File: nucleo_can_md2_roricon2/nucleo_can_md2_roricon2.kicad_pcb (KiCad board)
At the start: 2 copper layers, 63.7 x 58.6 mm, 24 parts, among them J1 Conn_01x05_Pin, J2 Conn_01x05_Pin, J3 Conn_01x02_Pin, U1 NUCLEO-F303K8, U2 MCP2562-E-P

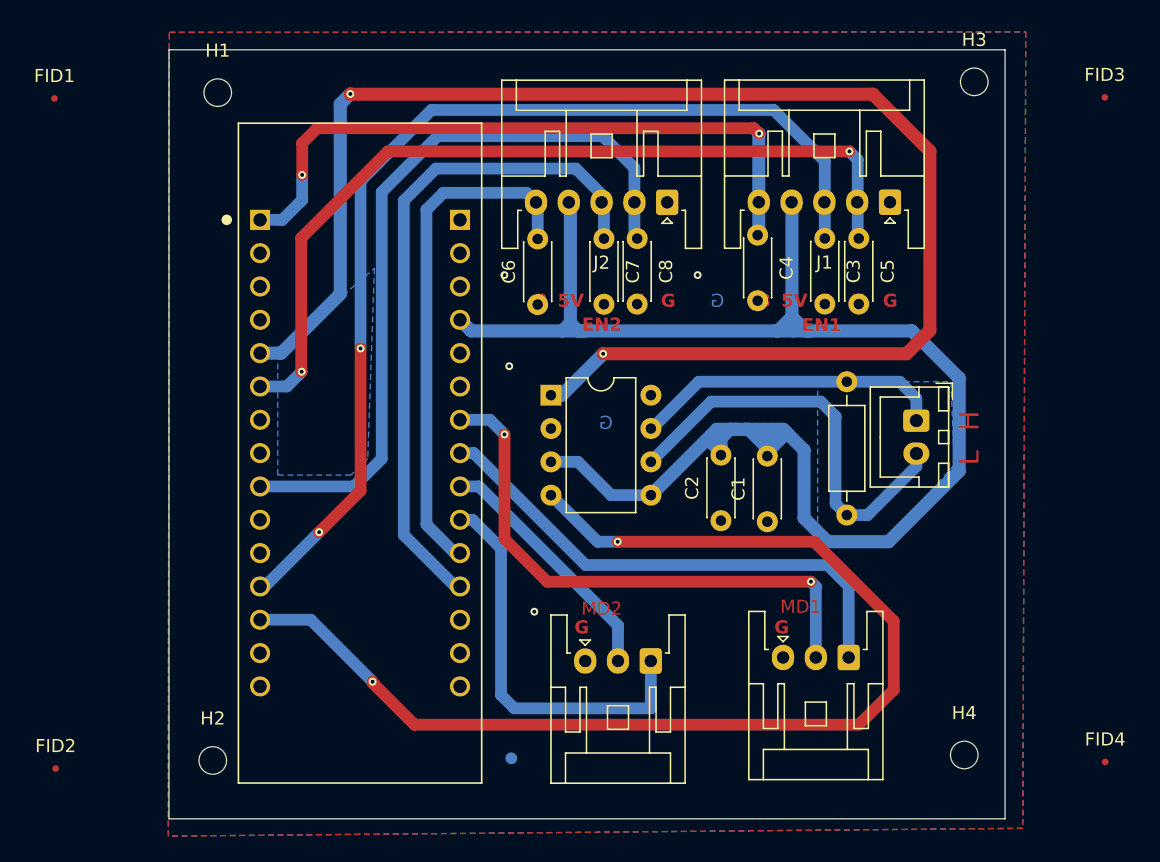
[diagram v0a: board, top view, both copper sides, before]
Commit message: feat:文字位置を修正
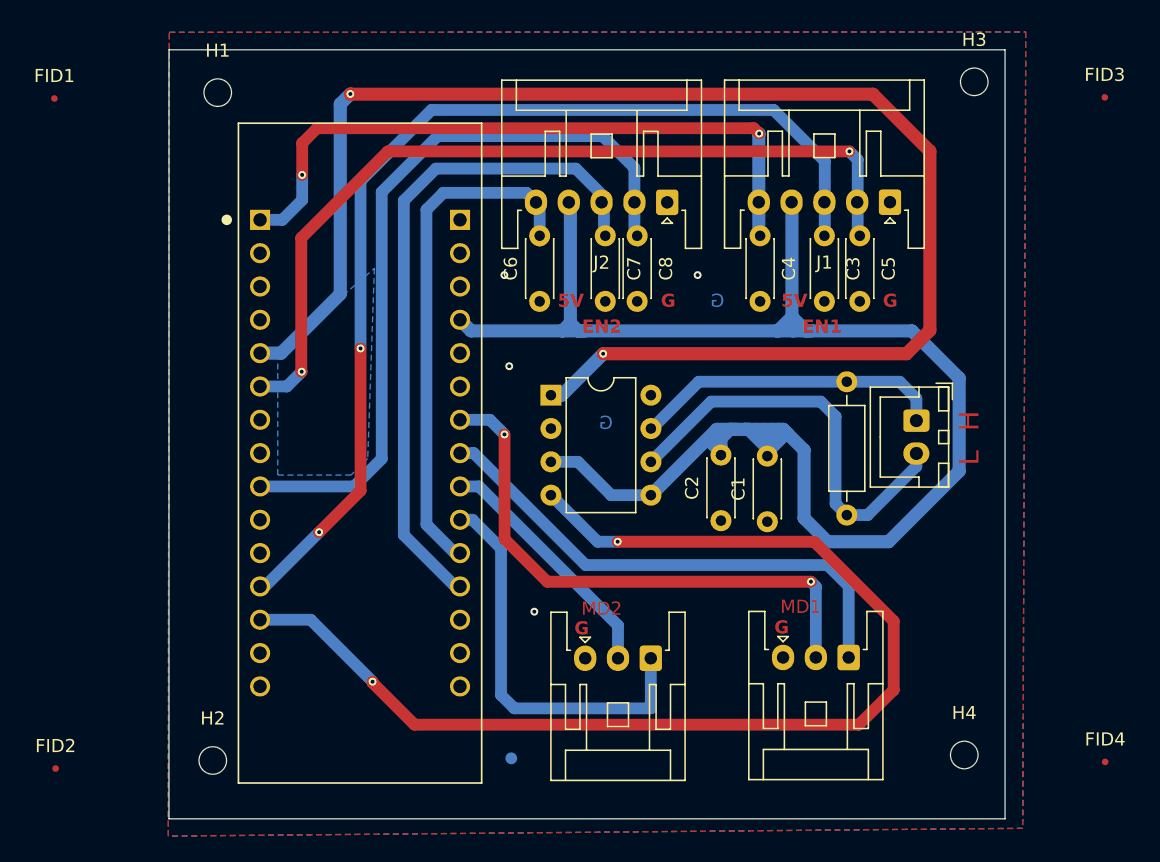
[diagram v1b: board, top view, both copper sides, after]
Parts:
- moved C6 0.29 mm to (142.9, 84.3)
- moved C7 0.24 mm to (147.9, 79.3)
- moved C5 0.22 mm to (167.3, 79.3)
- moved C8 0.21 mm to (150.3, 79.3)
- moved MD1 0.21 mm to (146.4, 111.5)
- moved C3 0.20 mm to (164.6, 79.3)
- moved C4 0.20 mm to (159.7, 79.3)
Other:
- board text removed: "A"
- board text removed: "B"
- board text removed: "X"
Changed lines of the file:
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@@
 	(footprint "Capacitor_THT:C_Disc_D4.3mm_W1.9mm_P5.00mm"
 		(layer "F.Cu")
-		(at 147.8 79.52 -90)
+		(at 147.9 79.3 -90)
 		(descr "C, Disc series, Radial, pin pitch=5.00mm, , diameter*width=4.3*1.9mm^2, Capacitor, http://www.vishay.com/docs/45233/krseries.pdf")
 		(tags "C Disc series Radial pin pitch 5.00mm  diameter 4.3mm width 1.9mm Capacitor")
@@
 	(footprint "Capacitor_THT:C_Disc_D4.3mm_W1.9mm_P5.00mm"
 		(layer "F.Cu")
-		(at 167.22 79.502 -90)
+		(at 167.3 79.3 -90)
 		(descr "C, Disc series, Radial, pin pitch=5.00mm, , diameter*width=4.3*1.9mm^2, Capacitor, http://www.vishay.com/docs/45233/krseries.pdf")
 		(tags "C Disc series Radial pin pitch 5.00mm  diameter 4.3mm width 1.9mm Capacitor")
@@
 			(at 2.5 2.2 -90)
 			(layer "F.Fab")
+			(hide yes)
 			(effects
 				(font
@@
 	(footprint "Capacitor_THT:C_Disc_D4.3mm_W1.9mm_P5.00mm"
 		(layer "F.Cu")
-		(at 142.748 84.542 90)
+		(at 142.9 84.3 90)
 		(descr "C, Disc series, Radial, pin pitch=5.00mm, , diameter*width=4.3*1.9mm^2, Capacitor, http://www.vishay.com/docs/45233/krseries.pdf")
 		(tags "C Disc series Radial pin pitch 5.00mm  diameter 4.3mm width 1.9mm Capacitor")
@@
 	(footprint "Capacitor_THT:C_Disc_D4.3mm_W1.9mm_P5.00mm"
 		(layer "F.Cu")
-		(at 150.33 79.51 -90)
+		(at 150.33 79.3 -90)
 		(descr "C, Disc series, Radial, pin pitch=5.00mm, , diameter*width=4.3*1.9mm^2, Capacitor, http://www.vishay.com/docs/45233/krseries.pdf")
 		(tags "C Disc series Radial pin pitch 5.00mm  diameter 4.3mm width 1.9mm Capacitor")
@@
 	(footprint "Capacitor_THT:C_Disc_D4.3mm_W1.9mm_P5.00mm"
 		(layer "F.Cu")
-		(at 159.512 79.248 -90)
+		(at 159.7 79.3 -90)
 		(descr "C, Disc series, Radial, pin pitch=5.00mm, , diameter*width=4.3*1.9mm^2, Capacitor, http://www.vishay.com/docs/45233/krseries.pdf")
 		(tags "C Disc series Radial pin pitch 5.00mm  diameter 4.3mm width 1.9mm Capacitor")
@@
 	(footprint "Capacitor_THT:C_Disc_D4.3mm_W1.9mm_P5.00mm"
 		(layer "F.Cu")
-		(at 164.63 79.502 -90)
+		(at 164.6 79.3 -90)
 		(descr "C, Disc series, Radial, pin pitch=5.00mm, , diameter*width=4.3*1.9mm^2, Capacitor, http://www.vishay.com/docs/45233/krseries.pdf")
 		(tags "C Disc series Radial pin pitch 5.00mm  diameter 4.3mm width 1.9mm Capacitor")
@@
 	(footprint "Connector_JST:JST_XA_S03B-XASK-1N-BN_1x03_P2.50mm_Horizontal"
 		(layer "F.Cu")
-		(at 146.37 111.71)
+		(at 146.37 111.5)
 		(descr "JST XA series connector, S03B-XASK-1N-BN (http://www.jst-mfg.com/product/pdf/eng/eXA1.pdf), generated with kicad-footprint-generator")
 		(tags "connector JST XA horizontal")
@@
 		(layer "Edge.Cuts")
 	)
-	(gr_text "B"
-		(at 160.528 84.836 0)
-		(layer "F.Cu" knockout)
-		(effects
-			(font
-				(size 1 1)
-				(thickness 0.2)
-			)
-			(justify right bottom)
-		)
-	)
 	(gr_text "G"
 		(at 153.26 84.836 0)
@@
 	)
 	(gr_text "EN2"
-		(at 146.12 86.65 0)
+		(at 146.12 86.8 0)
 		(layer "F.Cu" knockout)
 		(effects
@@
 		)
 	)
-	(gr_text "X"
-		(at 150.876 84.836 0)
-		(layer "F.Cu" knockout)
-		(effects
-			(font
-				(size 1 1)
-				(thickness 0.2)
-			)
-			(justify right bottom)
-		)
-	)
 	(gr_text "MD2"
 		(at 146.07 108.3 0)
@@
 	)
 	(gr_text "EN1"
-		(at 162.87 86.7 0)
+		(at 162.9 86.8 0)
 		(layer "F.Cu" knockout)
 		(effects
@@
 		)
 	)
-	(gr_text "A"
-		(at 148.336 84.836 0)
-		(layer "F.Cu" knockout)
-		(effects
-			(font
-				(size 1 1)
-				(thickness 0.2)
-			)
-			(justify right bottom)
-		)
-	)
 	(gr_text "G"
-		(at 145.542 109.728 0)
+		(at 145.542 109.8 0)
 		(layer "F.Cu" knockout)
 		(effects
@@
 		)
 	)
-	(gr_text "B"
-		(at 143.51 84.836 0)
-		(layer "F.Cu" knockout)
-		(effects
-			(font
-				(size 1 1)
-				(thickness 0.2)
-			)
-			(justify right bottom)
-		)
-	)
-	(gr_text "A"
-		(at 165.354 84.836 0)
-		(layer "F.Cu" knockout)
-		(effects
-			(font
-				(size 1 1)
-				(thickness 0.2)
-			)
-			(justify right bottom)
-		)
-	)
-	(gr_text "X"
-		(at 167.64 84.836 0)
-		(layer "F.Cu" knockout)
-		(effects
-			(font
-				(size 1 1)
-				(thickness 0.2)
-			)
-			(justify right bottom)
-		)
-	)
 	(gr_text "MD1"
 		(at 161.23 108.16 0)
@@
 	)
 	(segment
-		(start 147.695184 71.7)
-		(end 150.12 74.124816)
+		(start 128.755 98.405)
+		(end 130.86 96.3)
 		(width 0.9)
 		(layer "B.Cu")
@@
 	)
 	(segment
-		(start 128.755 98.405)
-		(end 130.86 96.3)
+		(start 135.13 71.7)
+		(end 147.695184 71.7)
 		(width 0.9)
 		(layer "B.Cu")
@@
 	)
 	(segment
-		(start 130.86 75.97)
-		(end 135.13 71.7)
+		(start 130.86 96.3)
+		(end 130.86 75.97)
 		(width 0.9)
 		(layer "B.Cu")
@@
 	)
 	(segment
-		(start 121.59 98.405)
-		(end 128.755 98.405)
+		(start 150.41 79.59)
+		(end 150.41 79.67)
 		(width 0.9)
 		(layer "B.Cu")
@@
 	)
 	(segment
-		(start 150.12 74.124816)
-		(end 150.12 79.3)
+		(start 121.59 98.405)
+		(end 128.755 98.405)
 		(width 0.9)
 		(layer "B.Cu")
@@
 	)
 	(segment
-		(start 135.13 71.7)
-		(end 147.695184 71.7)
+		(start 130.86 75.97)
+		(end 135.13 71.7)
 		(width 0.9)
 		(layer "B.Cu")
@@
 	)
 	(segment
-		(start 150.41 79.59)
-		(end 150.41 79.67)
+		(start 150.12 74.124816)
+		(end 150.12 79.3)
 		(width 0.9)
 		(layer "B.Cu")
@@
 	)
 	(segment
-		(start 150.12 79.3)
-		(end 150.41 79.59)
+		(start 147.695184 71.7)
+		(end 150.12 74.124816)
 		(width 0.9)
 		(layer "B.Cu")
@@
 	)
 	(segment
-		(start 130.86 96.3)
-		(end 130.86 75.97)
+		(start 150.12 79.3)
+		(end 150.41 79.59)
 		(width 0.9)
 		(layer "B.Cu")
@@
 	)
 	(segment
-		(start 135.5598 76.0247)
-		(end 134.27 77.3145)
+		(start 141.8947 76.0247)
+		(end 135.5598 76.0247)
 		(width 0.9)
 		(layer "B.Cu")
@@
 	)
 	(segment
-		(start 142.748 79.498)
-		(end 142.748 76.878)
+		(start 135.5598 76.0247)
+		(end 134.27 77.3145)
 		(width 0.9)
 		(layer "B.Cu")
@@
 	)
 	(segment
-		(start 142.748 76.878)
-		(end 141.8947 76.0247)
+		(start 142.92 79.67)
+		(end 142.9 79.65)
 		(width 0.9)
 		(layer "B.Cu")
@@
 	)
 	(segment
-		(start 134.27 77.3145)
-		(end 134.27 101.3115)
+		(start 136.4435 103.485)
+		(end 136.83 103.485)
 		(width 0.9)
 		(layer "B.Cu")
@@
 	)
 	(segment
-		(start 142.92 79.67)
-		(end 142.748 79.498)
+		(start 142.9 79.65)
+		(end 142.9 77.03)
 		(width 0.9)
 		(layer "B.Cu")
@@
 	)
 	(segment
-		(start 141.8947 76.0247)
-		(end 135.5598 76.0247)
+		(start 142.9 77.03)
+		(end 141.8947 76.0247)
 		(width 0.9)
 		(layer "B.Cu")
@@
 	)
 	(segment
-		(start 136.4435 103.485)
-		(end 136.83 103.485)
+		(start 134.27 77.3145)
+		(end 134.27 101.3115)
 		(width 0.9)
 		(layer "B.Cu")
@@
 		)
 	)
-	(zone
-		(net 0)
-		(net_name "")
-		(layer "B.Cu")
-		(hatch edge 0.5)
-		(priority 2)
-		(connect_pads
-			(clearance 1)
-		)
-		(min_thickness 0.25)
-		(filled_areas_thickness no)
-		(fill yes
-			(thermal_gap 0.5)
-			(thermal_bridge_width 0.5)
-			(island_removal_mode 1)
-			(island_area_min 10)
-		)
-		(polygon
-			(pts
-				(xy 164.084 90.424) (xy 174.244 90.424) (xy 174.498 96.774) (xy 169.418 102.362) (xy 164.846 102.362)
-				(xy 164.084 101.092)
-			)
-		)
+	(group ""
+		(members "13868a11-7ea7-494b-a1c7-75d396b34801")
 	)
 )

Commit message: 3.3v
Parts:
- C1, C2, C3, C4, C5, C6, C7, C8: value 0.1μ -> 0.01μ
- R1: footprint Resistor_THT:R_Axial_DIN0207_L6.3mm_D2.5mm_P10.16mm_Horizontal -> Resistor_THT:R_Axial_DIN0207_L6.3mm_D2.5mm_P2.54mm_Vertical
- moved C2 16.1 mm to (172.4, 104.2)
- moved C1 1.30 mm to (161.6, 101.1), turned to 180 degrees
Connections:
- C1 pad 2: +5V -> +3.3V
- U1 pad 4_14: unconnected-(U1B-+3V3-Pad4_14) -> +3.3V
- U2 pad 5: +5V -> +3.3V
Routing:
- net +3.3V: track 0.00 -> 39.3 mm, vias 0 -> 2
- net +5V: track 126.6 -> 111.8 mm
- net /L: track 32.1 -> 23.8 mm
- net MD1_dir: track 30.6 -> 29.3 mm
- net CAN_Rx: track 88.1 -> 86.9 mm, vias 2 -> 0
- net MD2_dir: track 39.3 -> 38.5 mm
- net GND: track 0.33 -> 0.31 mm, vias 4 -> 5
